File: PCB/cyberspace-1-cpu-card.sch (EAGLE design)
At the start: 26 parts, among them J1 Connector, 6P, SM, VT, J2 Connector, 6P, SM, VT, J3 Connector, 6P, SM, VT, J4 HEADER, FEMALE, 10P, U1 6502 Processor, U2 16V8, U3 16V8, U4 W65C22

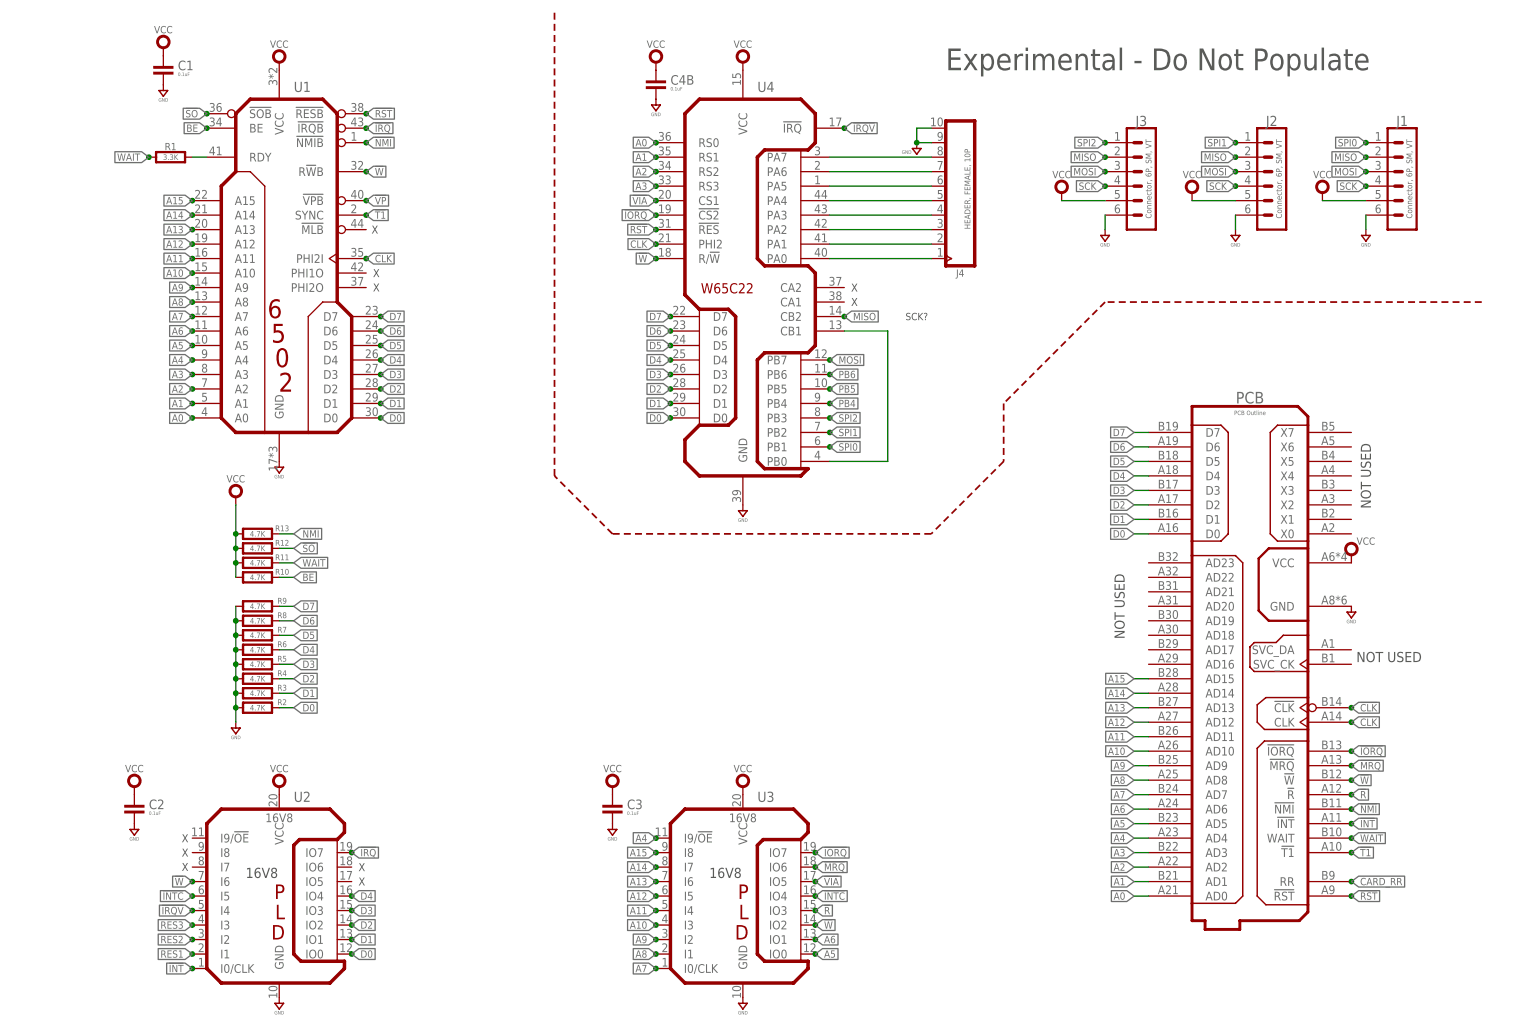
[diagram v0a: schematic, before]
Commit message: CPU PCB routed.
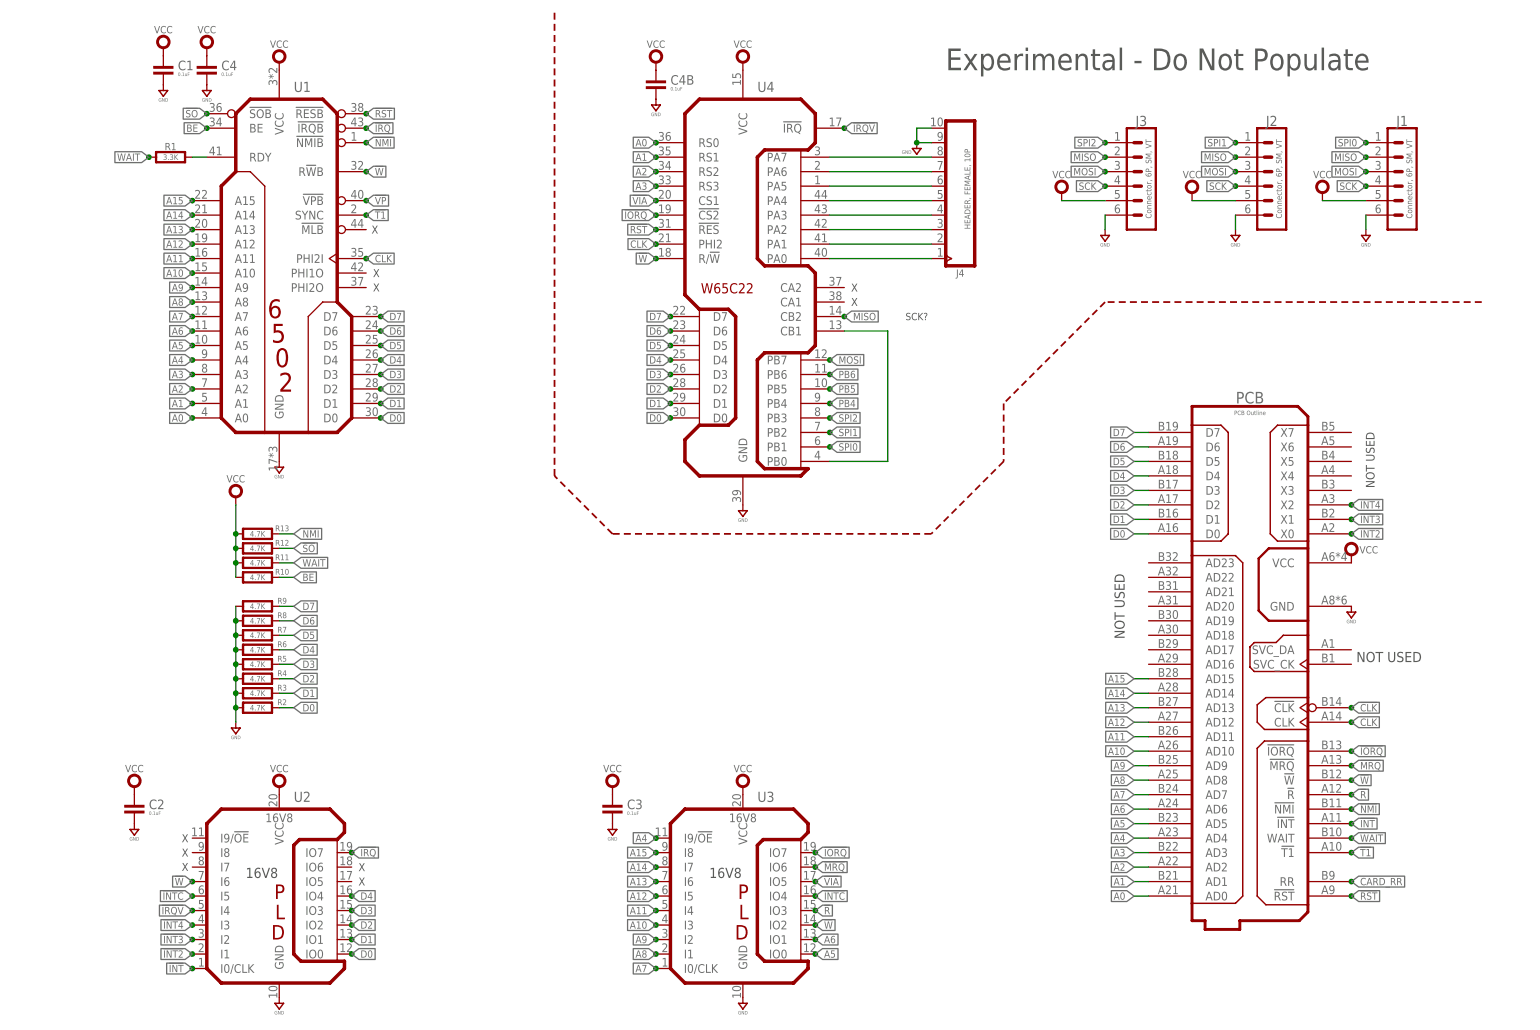
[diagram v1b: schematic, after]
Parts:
- added C4: 0.1uF, rlc:CAPACITOR0603
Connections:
- removed net RES1: U2.I1
- removed net RES2: U2.I2
- removed net RES3: U2.I3
- new net !INT2: PCB.X0, U2.I1
- new net !INT3: PCB.X1, U2.I2
- new net !INT4: PCB.X2, U2.I3
- net GND: now also C4.2
- net VCC: now also C4.1
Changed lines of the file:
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@@
 <part name="SUPPLY12" library="supply" library_urn="urn:adsk.eagle:library:10485988" deviceset="VCC" device=""/>
 <part name="R13" library="rlc" library_urn="urn:adsk.eagle:library:4192893" deviceset="RESISTOR" device="0603" package3d_urn="urn:adsk.eagle:package:4193040/5" value="4.7K"/>
+<part name="C4" library="rlc" library_urn="urn:adsk.eagle:library:4192893" deviceset="CAPACITOR" device="0603" package3d_urn="urn:adsk.eagle:package:4193021/4" value="0.1uF"/>
+<part name="SUPPLY28" library="supply" library_urn="urn:adsk.eagle:library:10485988" deviceset="VCC" device=""/>
+<part name="SUPPLY29" library="supply" library_urn="urn:adsk.eagle:library:10485988" deviceset="GND" device=""/>
 </parts>
 <sheets>
@@
 <text x="170.18" y="170.18" size="3.81" layer="97">Experimental - Do Not Populate</text>
 <text x="200.66" y="76.2" size="1.778" layer="97" rot="R90" align="center">NOT USED</text>
-<text x="243.84" y="99.06" size="1.778" layer="97" rot="R90" align="center">NOT USED</text>
+<text x="244.602" y="101.854" size="1.524" layer="97" rot="R90" align="center">NOT USED</text>
 <text x="247.904" y="67.31" size="1.778" layer="97" rot="R180" align="center">NOT USED</text>
 <text x="36.83" y="33.02" size="1.397" layer="97" distance="80" align="center">X
@@
 </instance>
 <instance part="SUPPLY13" gate="G$1" x="241.3" y="83.82" smashed="yes">
-<attribute name="VALUE" x="243.84" y="86.995" size="1.27" layer="96" font="vector" ratio="15" align="bottom-center"/>
+<attribute name="VALUE" x="244.348" y="85.471" size="1.27" layer="96" font="vector" ratio="15" align="bottom-center"/>
 </instance>
 <instance part="SUPPLY14" gate="G$1" x="134.62" y="170.18" smashed="yes">
@@
 <attribute name="NAME" x="53.848" y="89.3572" size="1.016" layer="95" font="vector" ratio="15" align="bottom-center"/>
 <attribute name="VALUE" x="49.53" y="88.9" size="0.9652" layer="96" font="vector" align="center"/>
+</instance>
+<instance part="C4" gate="G$1" x="40.64" y="170.18" smashed="yes">
+<attribute name="NAME" x="43.18" y="170.18" size="1.6764" layer="95" font="vector" ratio="15"/>
+<attribute name="VALUE" x="43.18" y="169.164" size="0.6096" layer="96" font="vector"/>
+</instance>
+<instance part="SUPPLY28" gate="G$1" x="40.64" y="172.72" smashed="yes">
+<attribute name="VALUE" x="40.64" y="176.657" size="1.27" layer="96" font="vector" ratio="15" align="bottom-center"/>
+</instance>
+<instance part="SUPPLY29" gate="GND" x="40.64" y="167.64" smashed="yes">
+<attribute name="VALUE" x="40.64" y="164.973" size="0.6096" layer="96" font="vector" align="center"/>
 </instance>
 </instances>
@@
 <pinref part="J1" gate="G$1" pin="6"/>
 </segment>
+<segment>
+<pinref part="C4" gate="G$1" pin="2"/>
+<pinref part="SUPPLY29" gate="GND" pin="GND"/>
+</segment>
 </net>
 <net name="VCC" class="0">
@@
 <pinref part="J1" gate="G$1" pin="5"/>
 </segment>
+<segment>
+<pinref part="C4" gate="G$1" pin="1"/>
+<pinref part="SUPPLY28" gate="G$1" pin="VCC"/>
+</segment>
 </net>
 <net name="N$1" class="0">
@@
 </segment>
 </net>
-<net name="RES1" class="0">
+<net name="!INT2" class="0">
 <segment>
 <pinref part="U2" gate="G$1" pin="I1"/>
@@
 <label x="38.1" y="15.24" size="1.27" layer="95" rot="R180" xref="yes"/>
 </segment>
-</net>
-<net name="RES2" class="0">
+<segment>
+<pinref part="PCB" gate="G$1" pin="X0"/>
+<junction x="241.3" y="88.9"/>
+<label x="241.3" y="88.9" size="1.27" layer="95" xref="yes"/>
+</segment>
+</net>
+<net name="!INT3" class="0">
 <segment>
 <pinref part="U2" gate="G$1" pin="I2"/>
@@
 <label x="38.1" y="17.78" size="1.27" layer="95" rot="R180" xref="yes"/>
 </segment>
-</net>
-<net name="RES3" class="0">
+<segment>
+<pinref part="PCB" gate="G$1" pin="X1"/>
+<junction x="241.3" y="91.44"/>
+<label x="241.3" y="91.44" size="1.27" layer="95" xref="yes"/>
+</segment>
+</net>
+<net name="!INT4" class="0">
 <segment>
 <pinref part="U2" gate="G$1" pin="I3"/>
@@
 <label x="38.1" y="20.32" size="1.27" layer="95" rot="R180" xref="yes"/>
 </segment>
-</net>
+<segment>
+<pinref part="PCB" gate="G$1" pin="X2"/>
+<junction x="241.3" y="93.98"/>
+<label x="241.3" y="93.98" size="1.27" layer="95" xref="yes"/>
+</segment>
+</net>

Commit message: GitHub did something weird. All new files and no idea why.
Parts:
- removed C4B: 0.1uF, rlc:CAPACITOR0603
- added C1B: 0.1uF, rlc:CAPACITOR0603
- added LED1, LED2, LED3, LED4: BLU, led:SMT0603
- added R14, R15, R16, R17: 470, rlc:RESISTOR0603
- added U$2: NO-FERMIUM-5MM, gfx-glyphs:NO-FERMIUM-5MM
- renumbered C1 to C1A
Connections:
- new net N$11: LED1.A, R14.1
- new net N$12: LED2.A, R15.1
- new net N$13: LED3.A, R16.1
- new net N$14: LED4.A, R17.1
- net !IRQ: now also PCB.X4
- net BE: now also PCB.X3
- net GND: now also C1B.2, LED1.C, LED2.C, LED3.C, LED4.C; no longer C4B.2
- net VCC: now also C1B.1, R14.2, R15.2, R16.2, R17.2; no longer C4B.1
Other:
- note added: "For probe only!"
- note added: "Test Point?"
- note added: "Used by Ram/Rom"
- note added: "Used by Rom programmer"
- moved on the sheet: C4
